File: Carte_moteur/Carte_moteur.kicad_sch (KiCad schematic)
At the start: 15 parts, among them J101 Conn_01x02_Socket, J102 Conn_01x02, J103 Conn_01x02, J104 Conn_01x07, U101 LD1117S33TR_SOT223

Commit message: updated motor PCB
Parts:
- added H101, H102, H103, H104: MountingHole_Pad, MountingHole:MountingHole_3.2mm_M3_DIN965_Pad, symbol Mechanical:MountingHole_Pad
- added J105: Conn_01x02_Socket, Connector_Molex:Molex_KK-396_A-41791-0002_1x02_P3.96mm_Vertical, symbol Connector:Conn_01x02_Socket
- added J106: Conn_01x07, Connector_Molex:Molex_KK-254_AE-6410-07A_1x07_P2.54mm_Vertical, symbol Connector_Generic:Conn_01x07
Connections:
- net +5V: now also J105.2 (Pin_2)
- net GND: now also H101.1, H102.1, H103.1, H104.1, J105.1 (Pin_1), J106.1 (Pin_1), J106.4 (Pin_4)
- net micro/LPUART1_RX: now also J106.2 (Pin_2)
- net micro/LPUART1_TX: now also J106.3 (Pin_3)
- net micro/SPI_MISO: now also J106.6 (Pin_6)
- net micro/SPI_MOSI: now also J106.7 (Pin_7)
- net micro/SPI_SCK: now also J106.5 (Pin_5)
- net micro/T_JDTI: now also J104.6 (Pin_6); no longer J104.7 (Pin_7)
- net micro/T_SWCLK: now also J104.5 (Pin_5); no longer J104.4 (Pin_4)
- net micro/T_SWDIO: now also J104.4 (Pin_4); no longer J104.5 (Pin_5)
- net micro/T_SWO: now also J104.7 (Pin_7); no longer J104.6 (Pin_6)
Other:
- moved on the sheet: C101, C102, C103, C104, C105, J101, J102, J103, J104, R101, R102, R103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

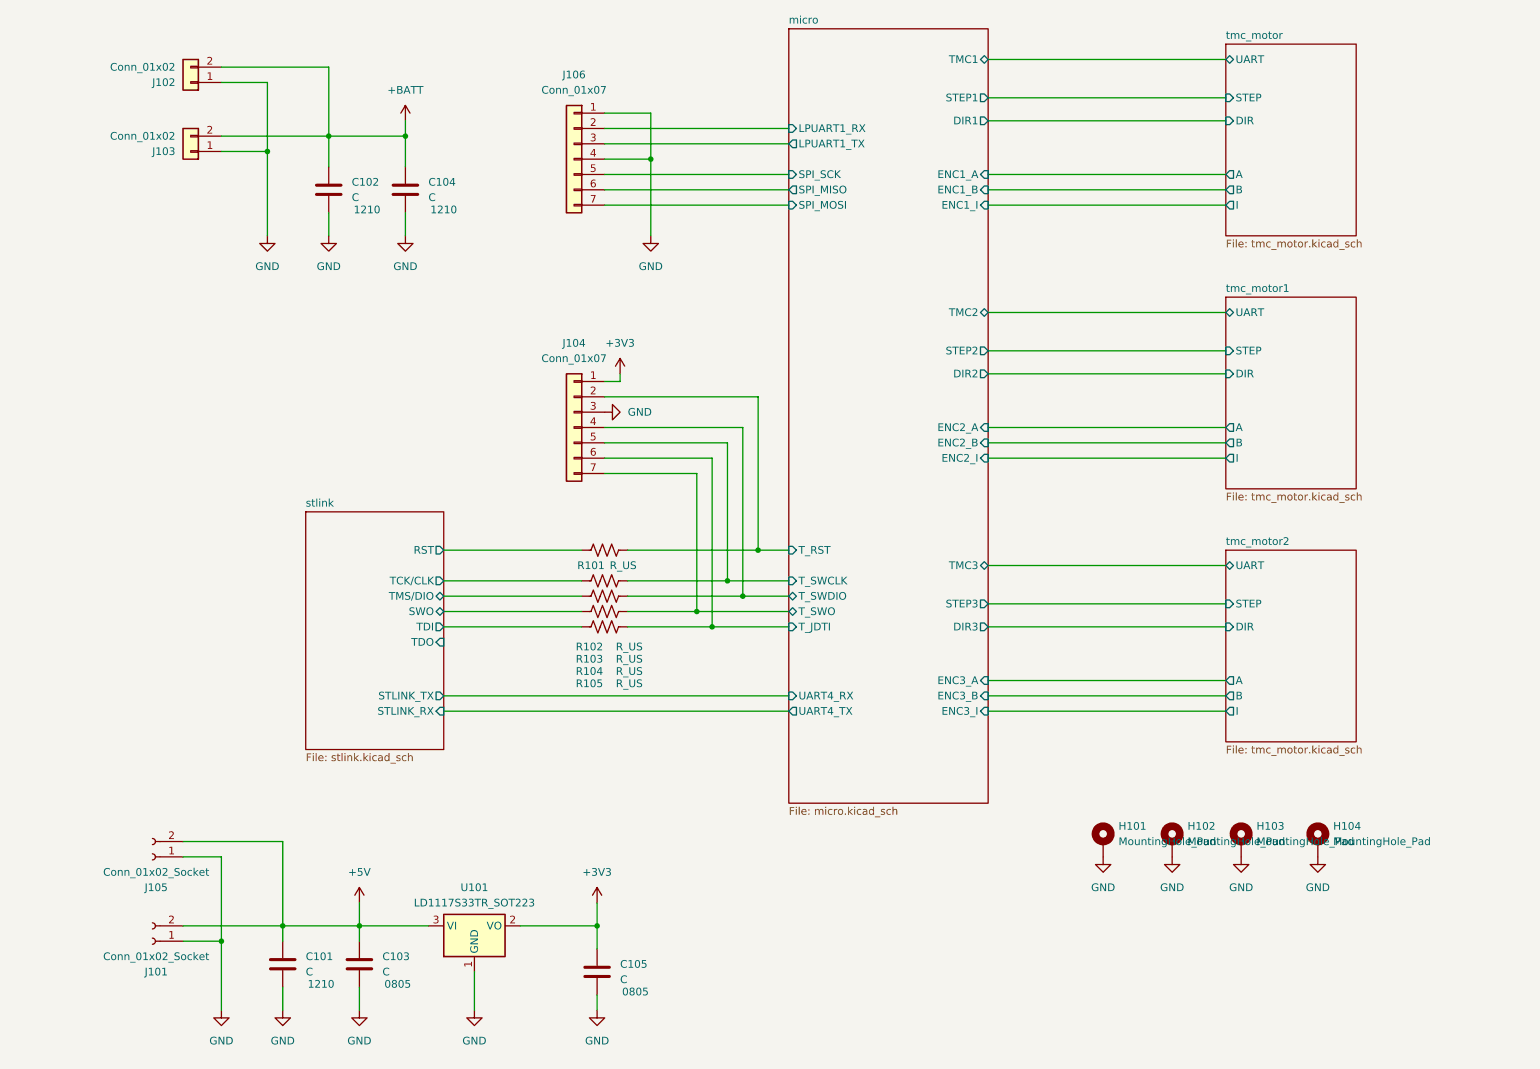
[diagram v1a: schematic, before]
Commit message: debug led added. Modified power connector
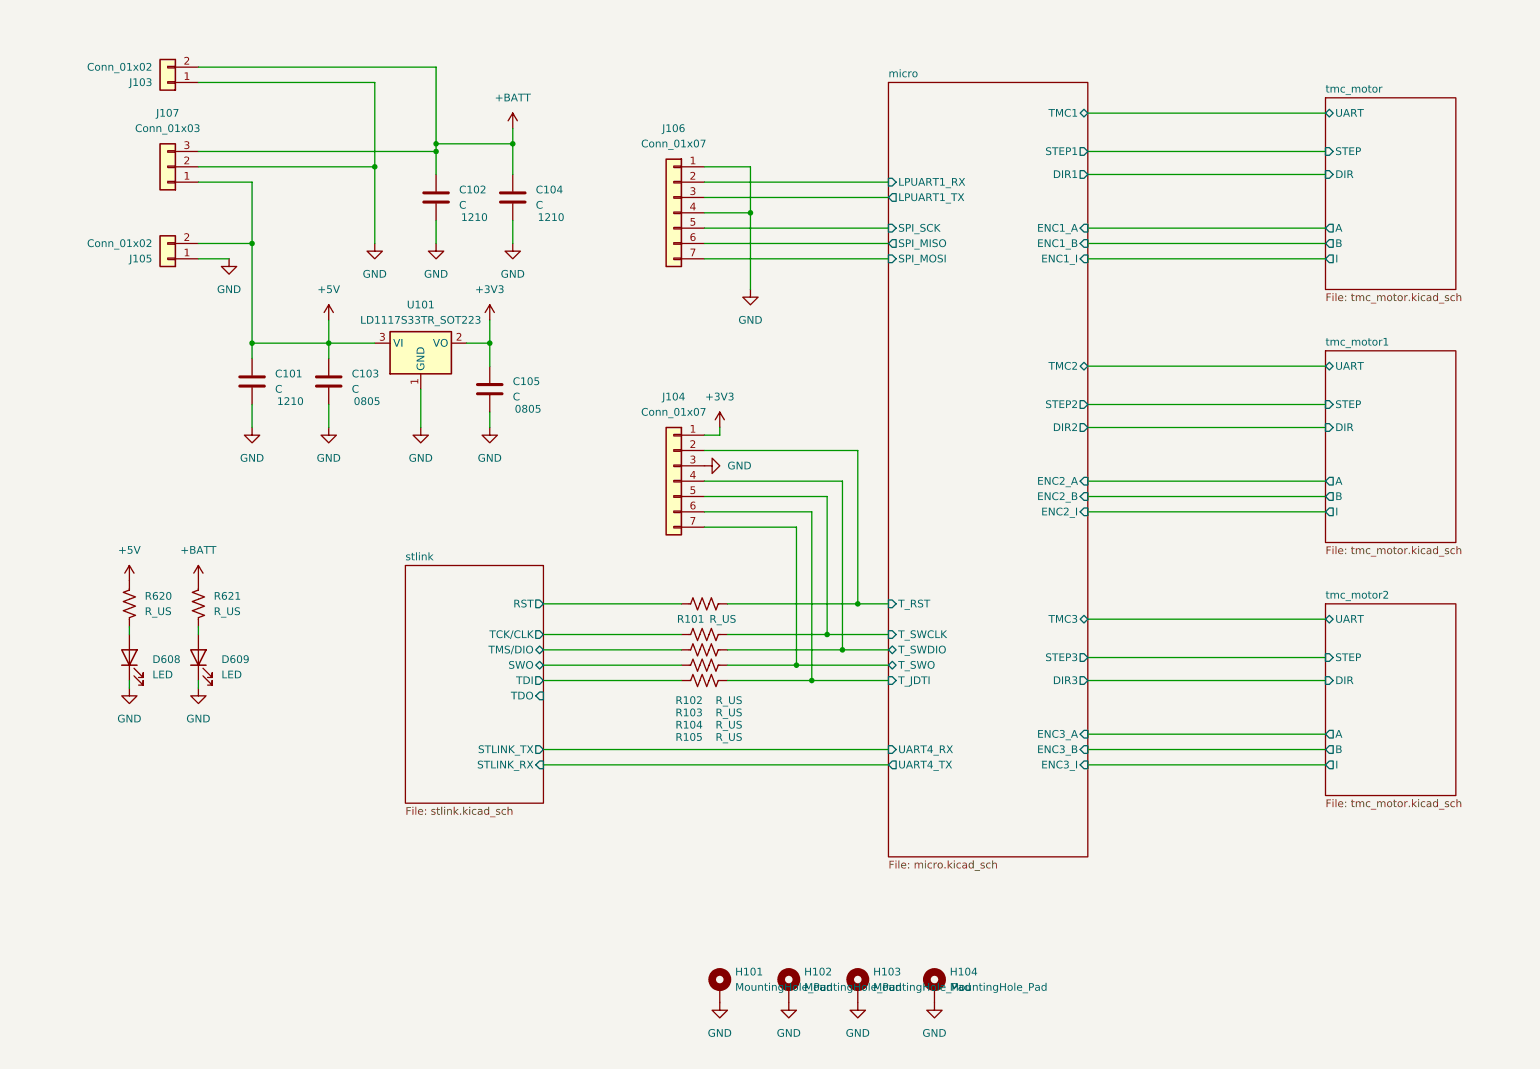
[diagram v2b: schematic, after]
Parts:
- removed J101, J105: Conn_01x02_Socket, Connector_Molex:Molex_KK-396_A-41791-0002_1x02_P3.96mm_Vertical, symbol Connector:Conn_01x02_Socket
- removed J102: Conn_01x02, Connector_Molex:Molex_KK-396_A-41791-0002_1x02_P3.96mm_Vertical, symbol Connector_Generic:Conn_01x02
- added D608, D609: LED, LED_SMD:LED_0805_2012Metric_Pad1.15x1.40mm_HandSolder, symbol Device:LED
- added J105: Conn_01x02, Connector_Molex:Molex_KK-396_A-41791-0002_1x02_P3.96mm_Vertical, symbol Connector_Generic:Conn_01x02
- added J107: Conn_01x03, Connector_Molex:Molex_KK-396_5273-03A_1x03_P3.96mm_Vertical, symbol Connector_Generic:Conn_01x03
- added R620, R621: R_US, Resistor_SMD:R_0603_1608Metric_Pad0.98x0.95mm_HandSolder, symbol Device:R_US
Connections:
- net +5V: now also J105.2 (Pin_2), J107.1 (Pin_1), R620.1
- net +BATT: now also J107.3 (Pin_3), R621.1
- net GND: now also D608.1 (K), D609.1 (K), J105.1 (Pin_1), J107.2 (Pin_2)
- new net: D608.2 (A), R620.2
- new net: D609.2 (A), R621.2
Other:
- moved on the sheet: C101, C102, C103, C104, C105, H101, H102, H103, H104, J103, J104, J106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

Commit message: changed pwr connector
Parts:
- removed J107: Conn_01x03, Connector_Molex:Molex_KK-396_5273-03A_1x03_P3.96mm_Vertical, symbol Connector_Generic:Conn_01x03
- added J101: Conn_02x04_Top_Bottom, Connector_Molex:Molex_Nano-Fit_105310-xx08_2x04_P2.50mm_Vertical, symbol Connector_Generic:Conn_02x04_Top_Bottom
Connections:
- net +5V: now also J101.7 (Pin_7)
- net +BATT: now also J101.1 (Pin_1), J101.5 (Pin_5)
- net GND: now also J101.4 (Pin_4), J101.8 (Pin_8)
- new net 12VL: J101.6 (Pin_6)
- new net 5VL: J101.3 (Pin_3)
- new net 9VL: J101.2 (Pin_2)
- no-connect marks 0 -> 4
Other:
- moved on the sheet: J103, J105

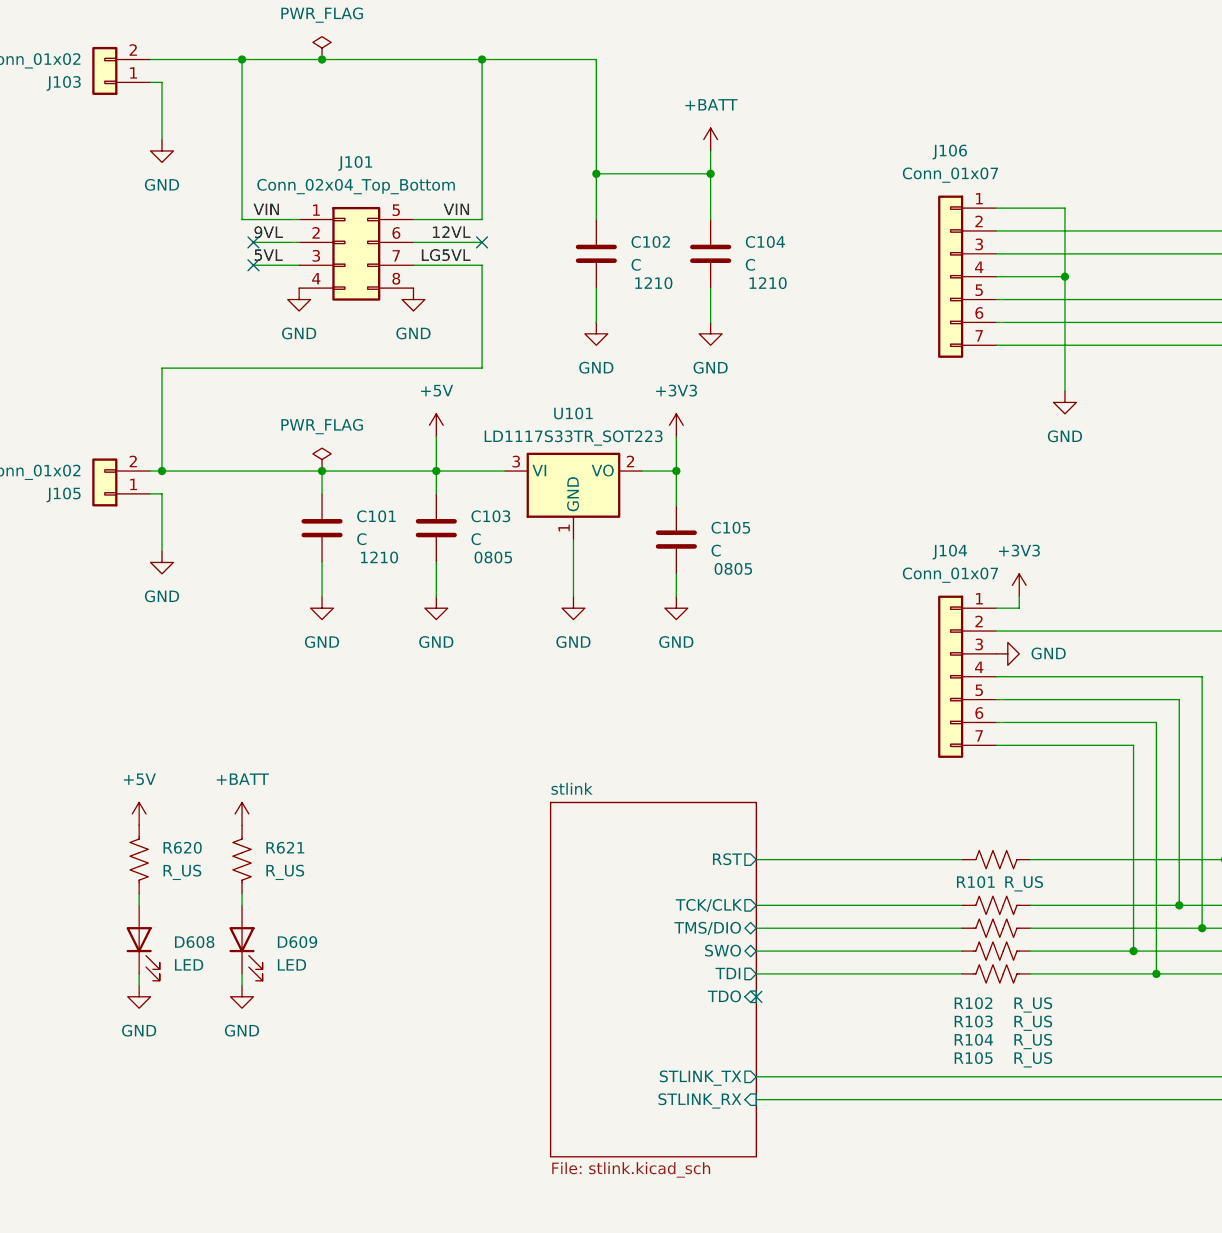
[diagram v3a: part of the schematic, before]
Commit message: update motor board values
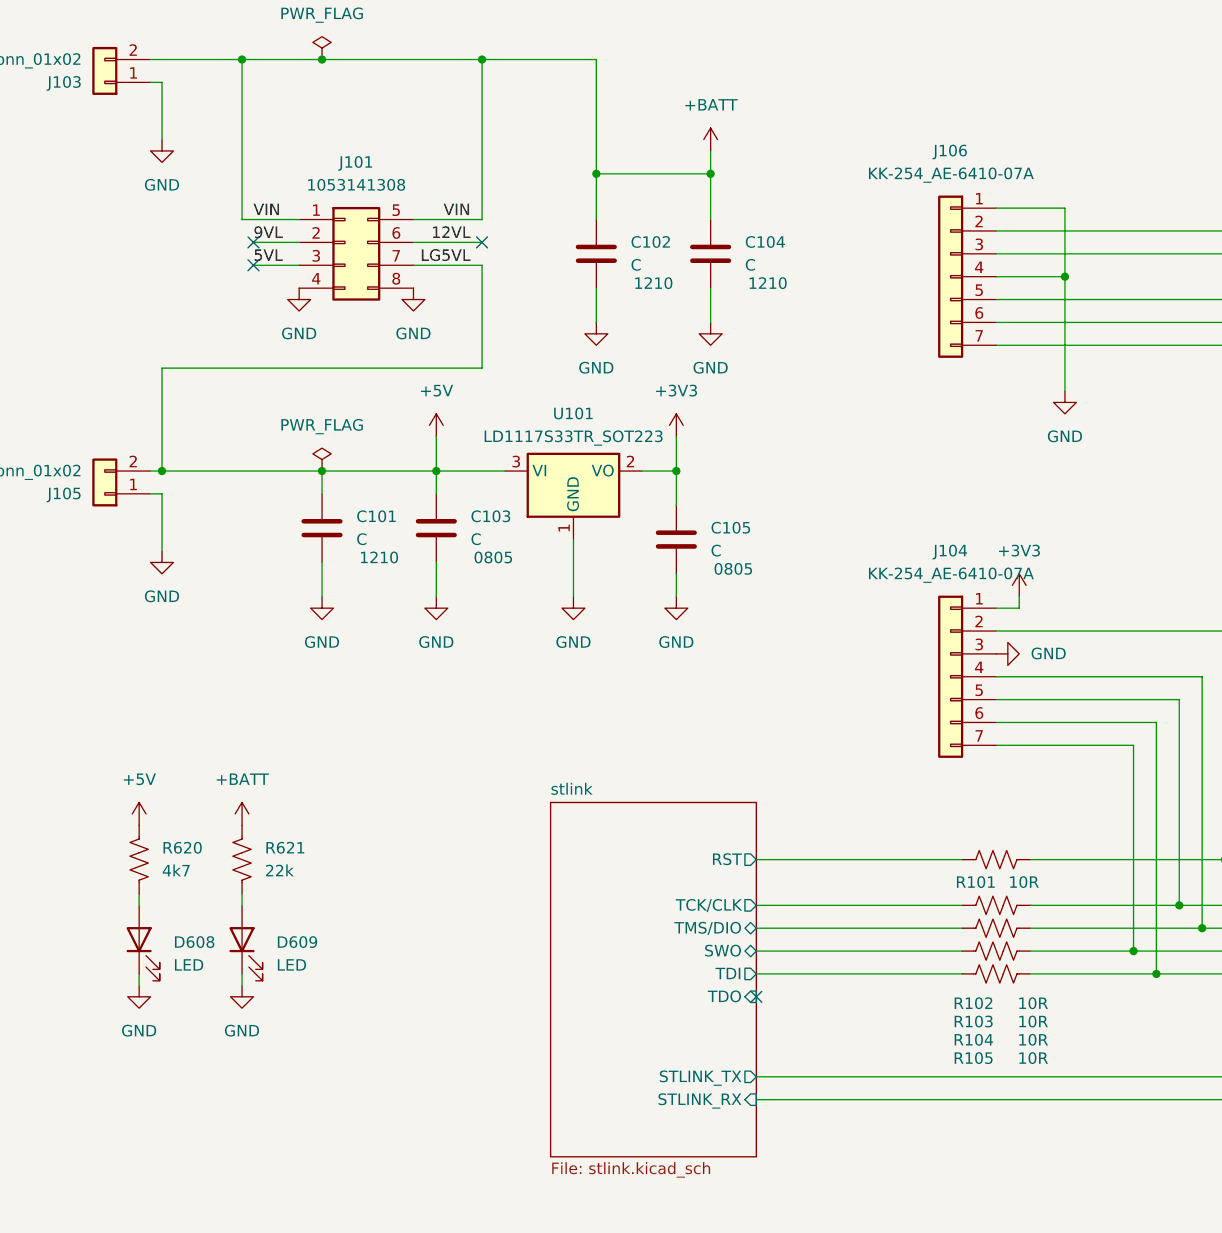
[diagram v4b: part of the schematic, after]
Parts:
- J101: value Conn_02x04_Top_Bottom -> 1053141308
- J104, J106: value Conn_01x07 -> KK-254_AE-6410-07A
- R101, R102, R103, R104, R105: value R_US -> 10R
- R620: value R_US -> 4k7
- R621: value R_US -> 22k
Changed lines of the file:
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@@
 			)
 		)
-		(property "Value" "R_US"
+		(property "Value" "4k7"
 			(at 33.02 118.1099 0)
 			(effects
@@
 			)
 		)
-		(property "Value" "Conn_01x07"
+		(property "Value" "KK-254_AE-6410-07A"
 			(at 120.65 85.09 0)
 			(effects
@@
 			)
 		)
-		(property "Value" "R_US"
+		(property "Value" "10R"
 			(at 129.794 138.938 90)
 			(effects
@@
 			)
 		)
-		(property "Value" "R_US"
+		(property "Value" "10R"
 			(at 129.794 136.906 90)
 			(effects
@@
 			)
 		)
-		(property "Value" "Conn_01x07"
+		(property "Value" "KK-254_AE-6410-07A"
 			(at 120.65 40.64 0)
 			(effects
@@
 			)
 		)
-		(property "Value" "R_US"
+		(property "Value" "10R"
 			(at 129.794 132.842 90)
 			(effects
@@
 			)
 		)
-		(property "Value" "R_US"
+		(property "Value" "22k"
 			(at 44.45 118.1099 0)
 			(effects
@@
 			)
 		)
-		(property "Value" "R_US"
+		(property "Value" "10R"
 			(at 128.778 119.38 90)
 			(effects
@@
 			)
 		)
-		(property "Value" "Conn_02x04_Top_Bottom"
+		(property "Value" "1053141308"
 			(at 54.61 41.91 0)
 			(effects
@@
 			)
 		)
-		(property "Value" "R_US"
+		(property "Value" "10R"
 			(at 129.794 134.874 90)
 			(effects
